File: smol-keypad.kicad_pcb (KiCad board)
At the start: 2 copper layers, 79.4 x 107.9 mm, 37 parts, among them U1 ProMicro

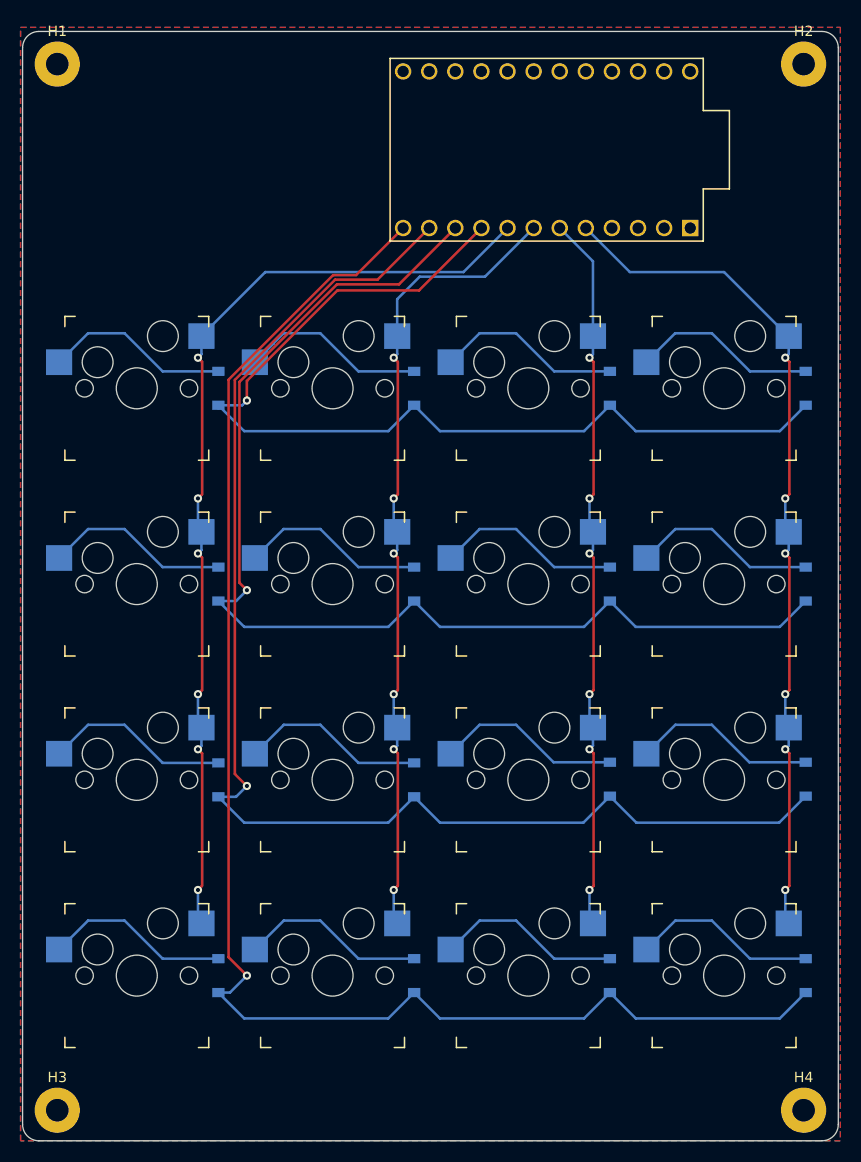
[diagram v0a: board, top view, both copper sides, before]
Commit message: add rotary encoders
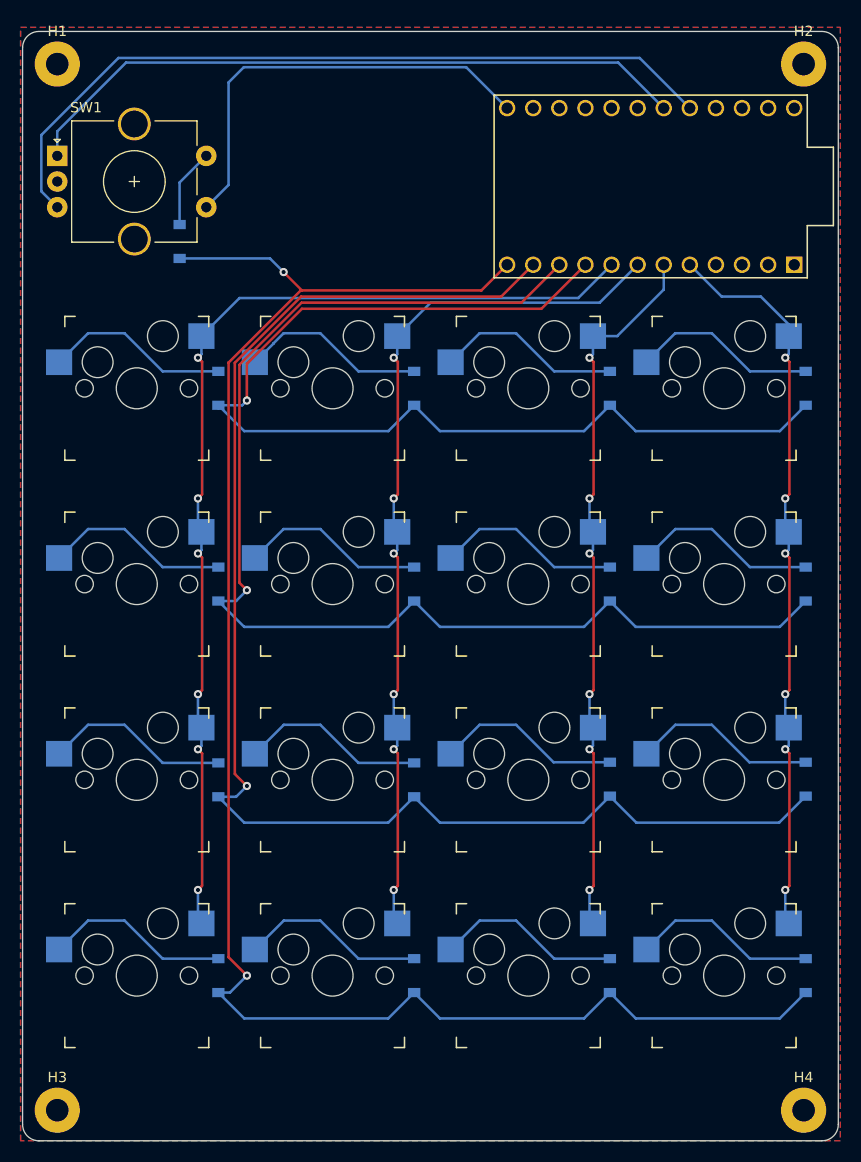
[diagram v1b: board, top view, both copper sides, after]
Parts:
- added D17: D_Small, Diode_SMD:D_SOD-123, B.Cu at (106.6, 48.2)
- added SW1: Rotary_Encoder_Switch, Rotary_Encoder:RotaryEncoder_Alps_EC11E-Switch_Vertical_H20mm_CircularMountingHoles, F.Cu at (94.7, 39.9)
- moved U1 10.7 mm to (152.4, 42.9)
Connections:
- U1 pad 13: Net-(U1-Pad13) -> /colRotEnc
- U1 pad 19: Net-(U1-Pad19) -> /pinA
- U1 pad 20: Net-(U1-Pad20) -> /pinB
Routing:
- net /pinB: track 0.00 -> 75.9 mm
- net /pinA: track 0.00 -> 66.0 mm
- net /colRotEnc: track 0.00 -> 42.4 mm
- net /row3: track 148.7 -> 171.5 mm, vias 1 -> 2
- net /col3: track 83.1 -> 72.2 mm
- net /row2: track 131.7 -> 141.3 mm
- net /row1: track 114.4 -> 124.0 mm
- net /row0: track 97.6 -> 107.2 mm
- net /col0: track 93.1 -> 101.8 mm
- net /rotEnc: track 0.00 -> 7.76 mm
- net /col1: track 78.7 -> 85.3 mm
- net /col2: track 70.8 -> 70.2 mm

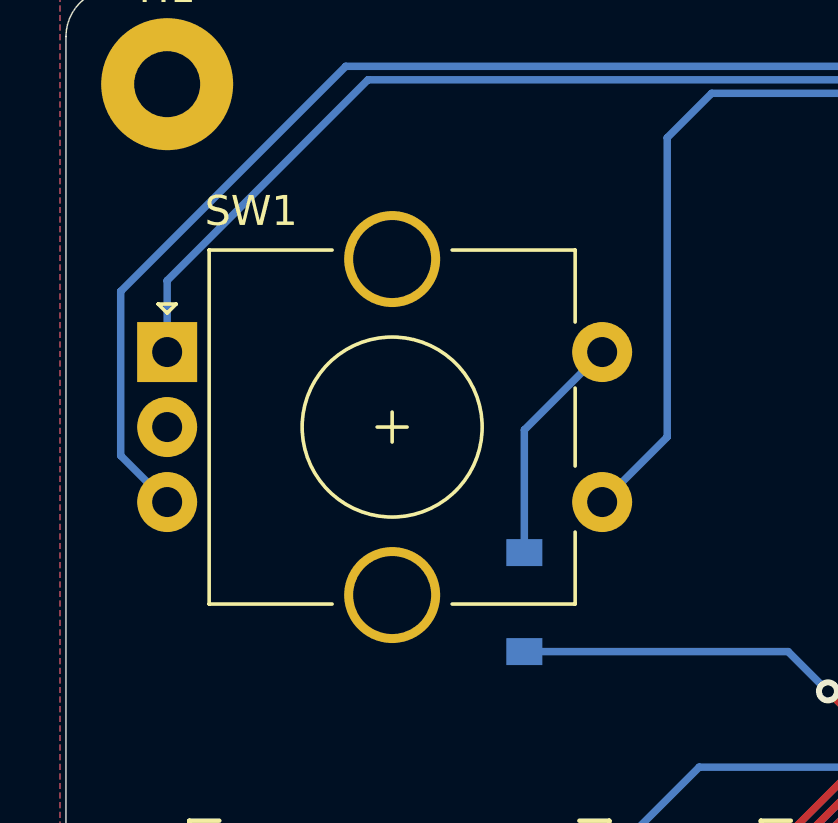
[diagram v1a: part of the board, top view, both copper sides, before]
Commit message: add kbd library
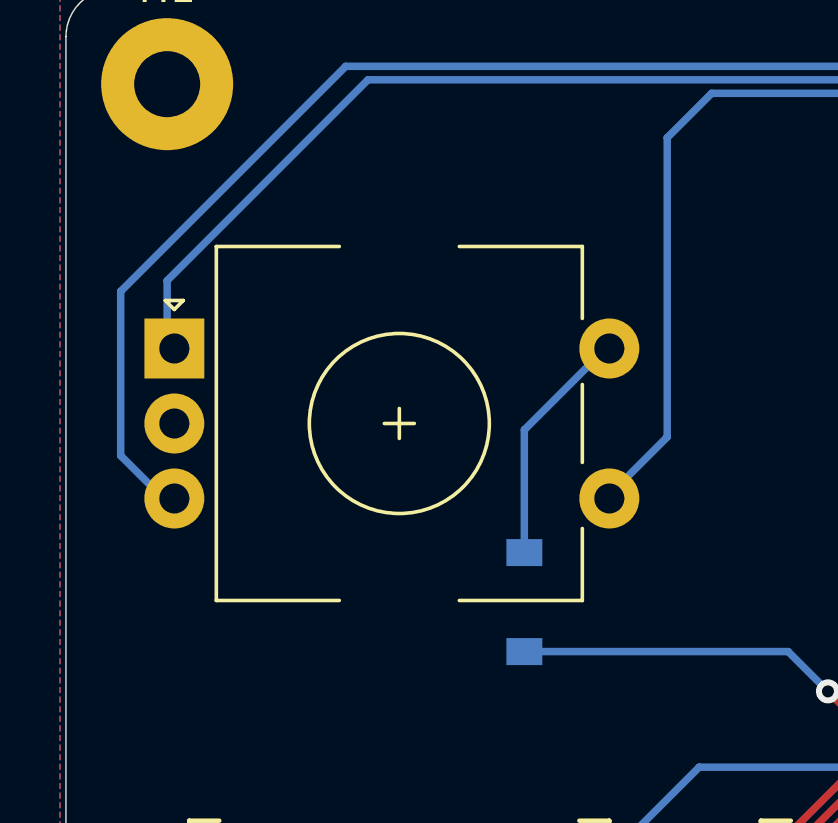
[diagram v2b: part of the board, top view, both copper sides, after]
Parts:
- SW1: footprint Rotary_Encoder:RotaryEncoder_Alps_EC11E-Switch_Vertical_H20mm_CircularMountingHoles -> Keebio-Parts:RotaryEncoder_EC11
- moved SW1 8.10 mm to (102.4, 42.3)
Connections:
- U1 pad 13: /colRotEnc -> Net-(U1-Pad13)
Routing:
- net Net-(U1-Pad13): track 0.00 -> 42.4 mm
- net /colRotEnc: track 42.4 -> 0.00 mm

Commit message: final
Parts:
- added OL1: OLED, kbd:OLED_v2, F.Cu at (119.1, 42.9)
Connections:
- U1 pad 13: Net-(U1-Pad13) -> /col2
- U1 pad 14: Net-(U1-Pad14) -> /col3
- U1 pad 15: Net-(U1-Pad15) -> /colRotEnc
- U1 pad 21: Net-(U1-Pad21) -> /VCC
- U1 pad 5: /col3 -> /SCL
- U1 pad 6: /col2 -> /SDA
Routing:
- net /col2: track 70.2 -> 126.5 mm
- net /SDA: track 0.00 -> 48.6 mm
- net /colRotEnc: track 0.00 -> 47.5 mm
- net /VCC: track 0.00 -> 43.4 mm
- net Net-(U1-Pad13): track 42.4 -> 0.00 mm
- net /SCL: track 0.00 -> 40.8 mm
- net /col3: track 72.2 -> 107.1 mm
